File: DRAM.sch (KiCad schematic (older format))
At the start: 38 parts, among them U1 MIMX8MM6DVTLZAA, U4 MT53B256M32D1NP-062 AIT:C TR

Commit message: Complete entry of bom
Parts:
- C1, C10, C11, C12, C18, C19, C2, C20, C21, C3, C4, C9: Mfgr (none) -> Murata; Part (none) -> GRM155C80J106ME11D; Vendorpart (none) -> 490-13233-1-ND
- C13, C14, C15, C16, C17, C22, C23, C24, C25, C26, C5, C6, C7, C8: Mfgr (none) -> Murata; Part (none) -> GRM155C8YA224ME01D; Vendorpart (none) -> 490-10446-1-ND
- R1, R2, R6: Mfgr (none) -> Yageo; Part (none) -> RC0402FR-07240RP; Vendorpart (none) -> YAG1258CT-ND
- R10, R9: Mfgr (none) -> Yageo; Part (none) -> RC0402FR-07150RL; Vendorpart (none) -> 311-150LRCT-ND
- R3, R5, R7, R8: value 10K -> 10K DNP; Part DNP -> (none)
- R4: Mfgr (none) -> Panasonic; Part (none) -> ERJ-2GEJ103X; Vendorpart (none) -> P10KJCT-ND
- U1: value MIMX8MM6DVTLZAA -> IMX8MM; Mfgr (none) -> NXP; Part (none) -> MIMX8MM6CVTKZAA; Vendorpart (none) -> 568-15276-ND
- U4: value MT53B256M32D1NP-062 AIT:C TR -> MT53E256M32D2DS-053 WT:B; Field4 MT53B256M32D1GZ-062 AIT:B -> (none); Field5 None -> (none); Field6 DRAM Chip Mobile LPDDR4 SDRAM 8G-Bit 256M x 32 1.1V 200-Pin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 -> (none); Field7 WFBGA-200 Micron -> (none); Field8 Micron Technology -> (none); Mfgr (none) -> Micron; Part (none) -> MT53E256M32D2DS-053 WT:B; Vendor (none) -> Mouser; Vendorpart (none) -> 340-359530

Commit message: Set up for battery NTC and add a power button
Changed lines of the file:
@@
 EESchema Schematic File Version 4
-LIBS:mxenc-cache
-EELAYER 29 0
+EELAYER 30 0
 EELAYER END
 $Descr USLedger 17000 11000
 encoding utf-8
 Sheet 2 10
-Title ""
-Date ""
-Rev ""
-Comp ""
+Title "kimχ micro"
+Date "2020-03-05"
+Rev "0.9"
+Comp "GroupGets"
 Comment1 ""
 Comment2 ""
@@
 $EndComp
 Wire Wire Line
-	8550 3850 8550 3750
-Wire Wire Line
 	8550 3750 8700 3750
 $Comp
@@
 NoConn ~ 2900 6200
 NoConn ~ 2900 5800
+Wire Wire Line
+	8550 3750 8550 3850
 $EndSCHEMATC

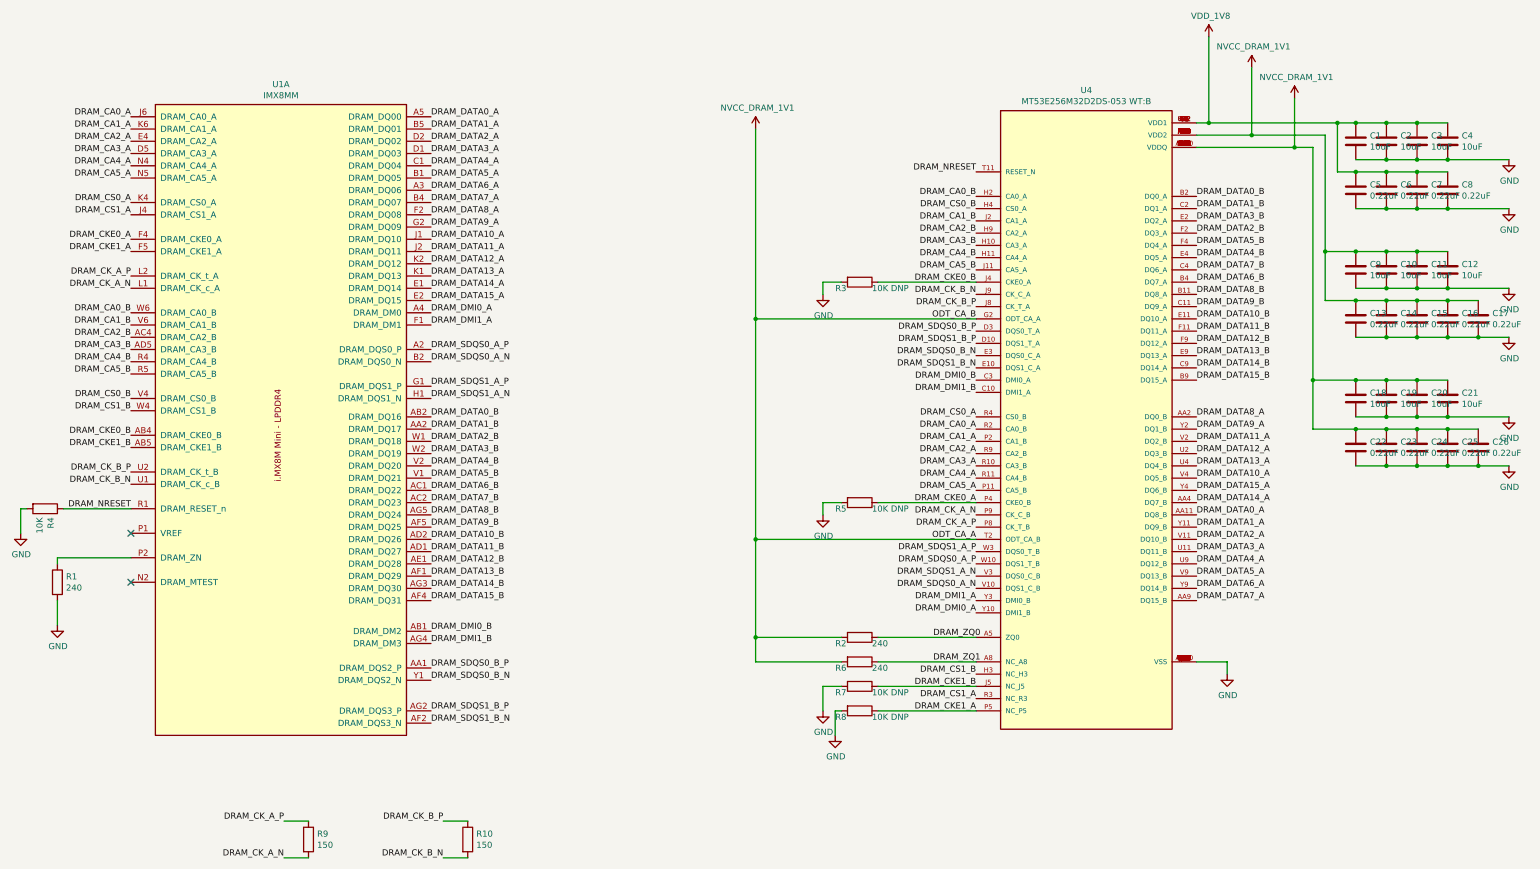
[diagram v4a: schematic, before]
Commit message: Re-annotate schematics, add dnp field, and silkscreen cleanup
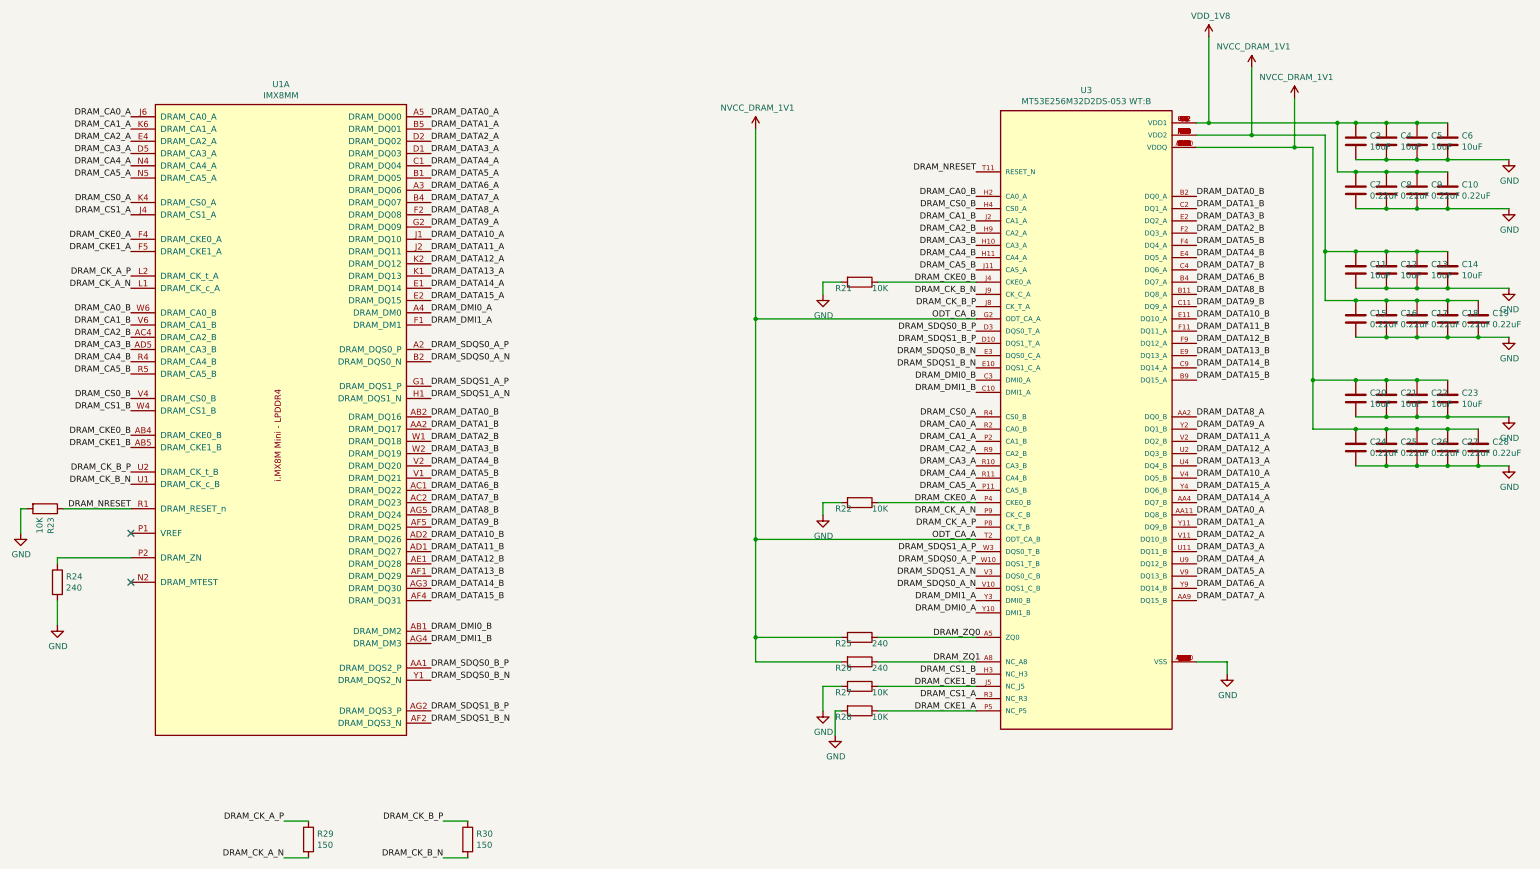
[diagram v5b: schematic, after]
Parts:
- R21: renamed from R3; value 10K DNP -> 10K; Mfgr (none) -> Panasonic; Part (none) -> ERJ-2GEJ103X; Populate (none) -> DNP; Vendorpart (none) -> P10KJCT-ND
- R22: renamed from R5; value 10K DNP -> 10K; Mfgr (none) -> Panasonic; Part (none) -> ERJ-2GEJ103X; Populate (none) -> DNP; Vendorpart (none) -> P10KJCT-ND
- R27: renamed from R7; value 10K DNP -> 10K; Mfgr (none) -> Panasonic; Part (none) -> ERJ-2GEJ103X; Populate (none) -> DNP; Vendorpart (none) -> P10KJCT-ND
- R28: renamed from R8; value 10K DNP -> 10K; Mfgr (none) -> Panasonic; Part (none) -> ERJ-2GEJ103X; Populate (none) -> DNP; Vendorpart (none) -> P10KJCT-ND
- renumbered C8 to C10, C9 to C11, C10 to C12, C11 to C13, C12 to C14, C13 to C15, C14 to C16, C15 to C17, C16 to C18, C17 to C19, C18 to C20, C19 to C21, C20 to C22, C21 to C23, C22 to C24, C23 to C25, C24 to C26, C25 to C27, C26 to C28, C1 to C3, C2 to C4, C3 to C5, C4 to C6, C5 to C7, C6 to C8, C7 to C9, R4 to R23, R1 to R24, R2 to R25, R6 to R26, R9 to R29, R10 to R30, U4 to U3

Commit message: Fixed a few comments related to component reference and make sure we're displaying dnp
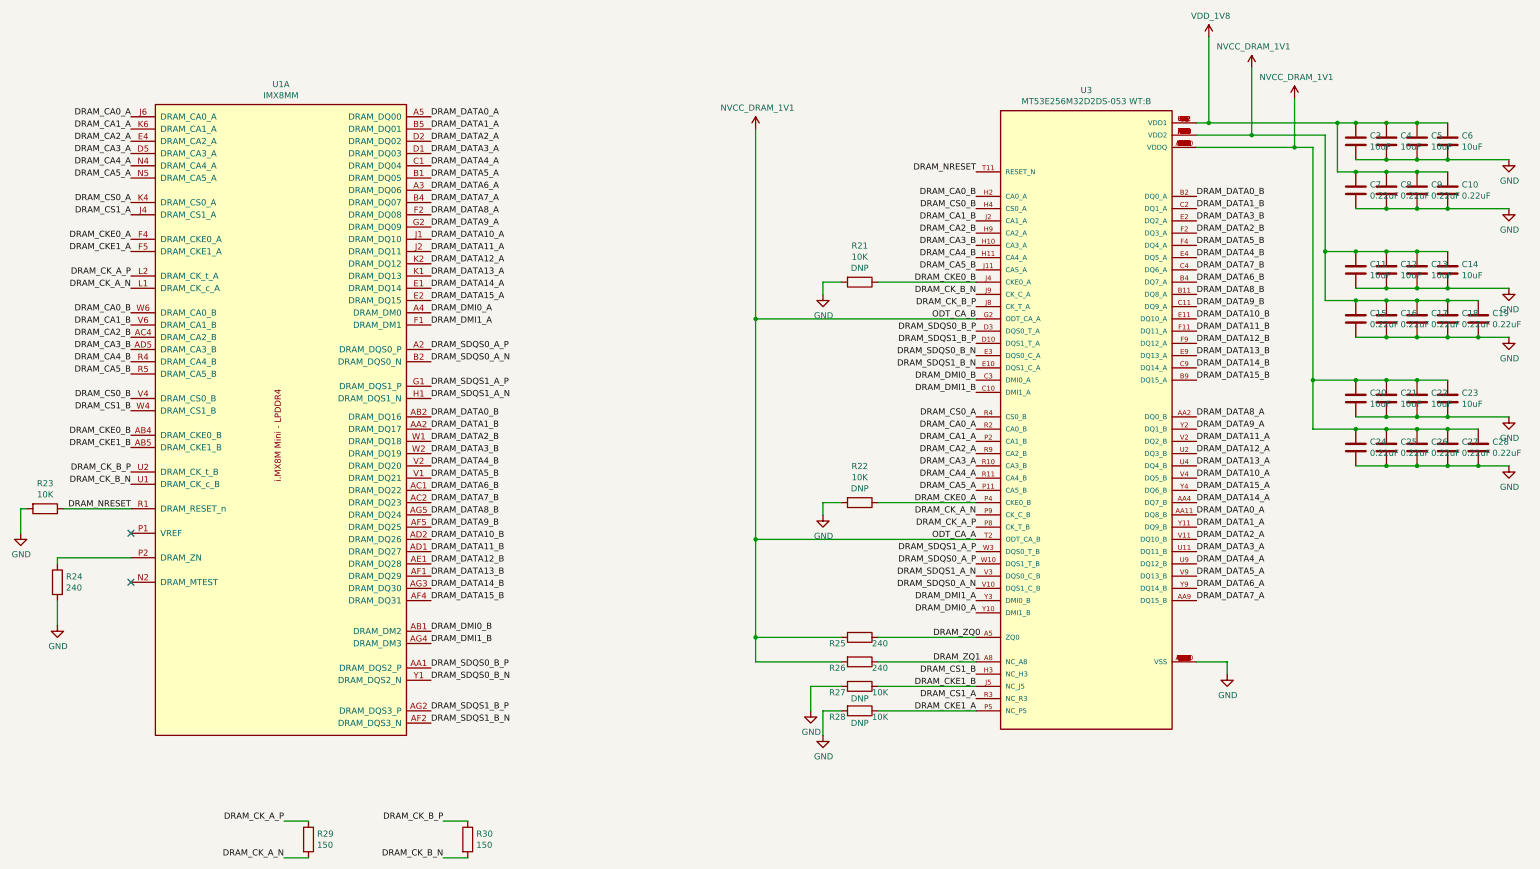
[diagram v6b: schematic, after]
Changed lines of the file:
@@
 U 1 1 5CFE0CF7
 P 8850 6850
-F 0 "R26" V 8900 6650 50  0000 L CNN
+F 0 "R26" V 8900 6600 50  0000 L CNN
 F 1 "240" V 8900 6950 50  0000 L CNN
 F 2 "Resistor_SMD:R_0402_1005Metric" V 8780 6850 50  0001 C CNN
@@
 U 1 1 5CFECAE2
 P 8850 3750
-F 0 "R21" V 8900 3550 50  0000 L CNN
-F 1 "10K" V 8900 3850 50  0000 L CNN
+F 0 "R21" V 8553 3750 50  0000 C CNN
+F 1 "10K" V 8644 3750 50  0000 C CNN
 F 2 "Resistor_SMD:R_0402_1005Metric" V 8780 3750 50  0001 C CNN
 F 3 "~" H 8850 3750 50  0001 C CNN
 F 4 "Panasonic" H 8850 3750 50  0001 C CNN "Mfgr"
 F 5 "ERJ-2GEJ103X" H 8850 3750 50  0001 C CNN "Part"
-F 6 "DNP" H 8850 3750 50  0001 C CNN "Populate"
+F 6 "DNP" V 8735 3750 50  0000 C CNN "Populate"
 F 7 "P10KJCT-ND" H 8850 3750 50  0001 C CNN "Vendorpart"
 	1    8850 3750
@@
 U 1 1 5CFE8153
 P 2200 5600
-F 0 "R23" H 2270 5646 50  0000 L CNN
-F 1 "10K" H 2270 5555 50  0000 L CNN
+F 0 "R23" V 1993 5600 50  0000 C CNN
+F 1 "10K" V 2084 5600 50  0000 C CNN
 F 2 "Resistor_SMD:R_0402_1005Metric" V 2130 5600 50  0001 C CNN
 F 3 "~" H 2200 5600 50  0001 C CNN
@@
 U 1 1 5CFF10F6
 P 8850 7050
-F 0 "R27" V 8900 6850 50  0000 L CNN
+F 0 "R27" V 8900 6800 50  0000 L CNN
 F 1 "10K" V 8900 7150 50  0000 L CNN
 F 2 "Resistor_SMD:R_0402_1005Metric" V 8780 7050 50  0001 C CNN
@@
 F 4 "Panasonic" H 8850 7050 50  0001 C CNN "Mfgr"
 F 5 "ERJ-2GEJ103X" H 8850 7050 50  0001 C CNN "Part"
-F 6 "DNP" H 8850 7050 50  0001 C CNN "Populate"
+F 6 "DNP" V 8950 7050 50  0000 C CNN "Populate"
 F 7 "P10KJCT-ND" H 8850 7050 50  0001 C CNN "Vendorpart"
 	1    8850 7050
@@
 L power:GND #PWR047
 U 1 1 5CFF10FD
-P 8550 7250
-F 0 "#PWR047" H 8550 7000 50  0001 C CNN
-F 1 "GND" H 8555 7077 50  0000 C CNN
-F 2 "" H 8550 7250 50  0001 C CNN
-F 3 "" H 8550 7250 50  0001 C CNN
-	1    8550 7250
-	1    0    0    -1
-$EndComp
-Wire Wire Line
-	8550 7250 8550 7050
-Wire Wire Line
-	8550 7050 8700 7050
+P 8450 7250
+F 0 "#PWR047" H 8450 7000 50  0001 C CNN
+F 1 "GND" H 8455 7077 50  0000 C CNN
+F 2 "" H 8450 7250 50  0001 C CNN
+F 3 "" H 8450 7250 50  0001 C CNN
+	1    8450 7250
+	1    0    0    -1
+$EndComp
+Wire Wire Line
+	8450 7250 8450 7050
+Wire Wire Line
+	8450 7050 8700 7050
 $Comp
 L Device:R R22
 U 1 1 5CFF3BC1
 P 8850 5550
-F 0 "R22" V 8900 5350 50  0000 L CNN
-F 1 "10K" V 8900 5650 50  0000 L CNN
+F 0 "R22" V 8553 5550 50  0000 C CNN
+F 1 "10K" V 8644 5550 50  0000 C CNN
 F 2 "Resistor_SMD:R_0402_1005Metric" V 8780 5550 50  0001 C CNN
 F 3 "~" H 8850 5550 50  0001 C CNN
 F 4 "Panasonic" H 8850 5550 50  0001 C CNN "Mfgr"
 F 5 "ERJ-2GEJ103X" H 8850 5550 50  0001 C CNN "Part"
-F 6 "DNP" H 8850 5550 50  0001 C CNN "Populate"
+F 6 "DNP" V 8735 5550 50  0000 C CNN "Populate"
 F 7 "P10KJCT-ND" H 8850 5550 50  0001 C CNN "Vendorpart"
 	1    8850 5550
@@
 U 1 1 5CFF565A
 P 8850 7250
-F 0 "R28" V 8900 7050 50  0000 L CNN
+F 0 "R28" V 8900 7000 50  0000 L CNN
 F 1 "10K" V 8900 7350 50  0000 L CNN
 F 2 "Resistor_SMD:R_0402_1005Metric" V 8780 7250 50  0001 C CNN
@@
 F 4 "Panasonic" H 8850 7250 50  0001 C CNN "Mfgr"
 F 5 "ERJ-2GEJ103X" H 8850 7250 50  0001 C CNN "Part"
-F 6 "DNP" H 8850 7250 50  0001 C CNN "Populate"
+F 6 "DNP" V 8950 7250 50  0000 C CNN "Populate"
 F 7 "P10KJCT-ND" H 8850 7250 50  0001 C CNN "Vendorpart"
 	1    8850 7250
@@
 L power:GND #PWR048
 U 1 1 5CFF5661
-P 8650 7450
-F 0 "#PWR048" H 8650 7200 50  0001 C CNN
-F 1 "GND" H 8655 7277 50  0000 C CNN
-F 2 "" H 8650 7450 50  0001 C CNN
-F 3 "" H 8650 7450 50  0001 C CNN
-	1    8650 7450
-	1    0    0    -1
-$EndComp
-Wire Wire Line
-	8700 7250 8650 7250
-Wire Wire Line
-	8650 7250 8650 7450
+P 8550 7450
+F 0 "#PWR048" H 8550 7200 50  0001 C CNN
+F 1 "GND" H 8555 7277 50  0000 C CNN
+F 2 "" H 8550 7450 50  0001 C CNN
+F 3 "" H 8550 7450 50  0001 C CNN
+	1    8550 7450
+	1    0    0    -1
+$EndComp
+Wire Wire Line
+	8700 7250 8550 7250
+Wire Wire Line
+	8550 7250 8550 7450
 Text Label 5350 4400 0    50   ~ 0
 DRAM_SDQS0_A_N
@@
 U 1 1 5D00DB12
 P 8850 6650
-F 0 "R25" V 8900 6450 50  0000 L CNN
+F 0 "R25" V 8900 6400 50  0000 L CNN
 F 1 "240" V 8900 6750 50  0000 L CNN
 F 2 "Resistor_SMD:R_0402_1005Metric" V 8780 6650 50  0001 C CNN
